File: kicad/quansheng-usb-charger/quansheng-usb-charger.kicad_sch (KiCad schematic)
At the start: 29 parts, among them J1 USB_C_Receptacle_USB2.0, U1 IP2326

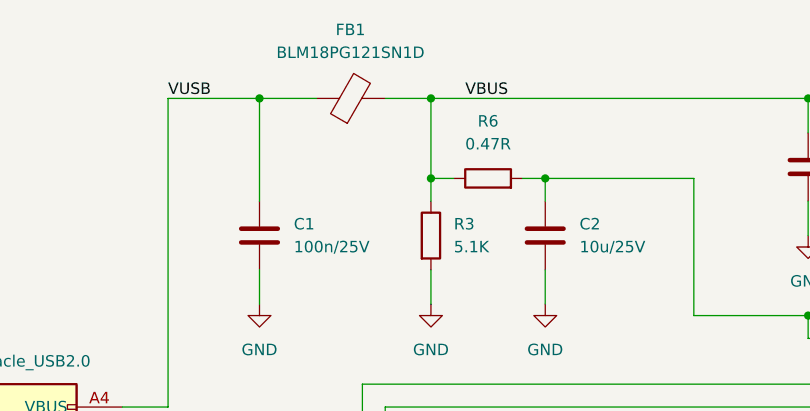
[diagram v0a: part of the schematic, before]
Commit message: Add JLCPCB files and README
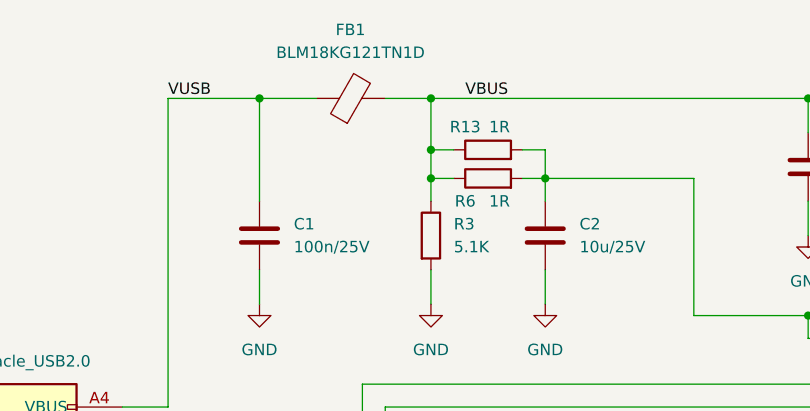
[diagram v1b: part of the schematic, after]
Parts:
- added R13: 1R, Resistor_SMD:R_0603_1608Metric, symbol Device:R
- C1, C4: LCSC (none) -> C14663
- C2, C3, C7, C8: LCSC (none) -> C15850
- C5, C6: LCSC (none) -> C45783
- FB1: value BLM18PG121SN1D -> BLM18KG121TN1D; LCSC (none) -> C85831
- J1: LCSC (none) -> C2988369
- L1: LCSC (none) -> C177247
- R1, R2, R3: LCSC (none) -> C23186
- R11: LCSC (none) -> C23196
- R12, R8, R9: LCSC (none) -> C25808
- R5, R7: LCSC (none) -> C21190
- R6: value 0.47R -> 1R; LCSC (none) -> C22936
- U1: LCSC (none) -> C2832094
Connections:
- net VBUS: now also R13.1
- net at C2.1, R6.2, U1.12 (EN)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: now also R13.2
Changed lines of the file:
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@@
   (junction (at 193.04 63.5) (diameter 0) (color 0 0 0 0)
   )
+  (junction (at 95.25 50.165) (diameter 0) (color 0 0 0 0)
+  )
   (junction (at 95.25 44.45) (diameter 0) (color 0 0 0 0)
   )
@@
     (stroke (width 0) (type default) (color 0 0 0 0))
   )
-  (wire (pts (xy 95.25 44.45) (xy 95.25 53.34))
+  (wire (pts (xy 95.25 44.45) (xy 95.25 50.165))
     (stroke (width 0) (type default) (color 0 0 0 0))
   )
@@
     (stroke (width 0) (type default) (color 0 0 0 0))
   )
+  (wire (pts (xy 95.25 50.165) (xy 97.79 50.165))
+    (stroke (width 0) (type default) (color 0 0 0 0))
+  )
   (wire (pts (xy 121.92 120.65) (xy 121.92 123.19))
     (stroke (width 0) (type default) (color 0 0 0 0))
@@
     (stroke (width 0) (type default) (color 0 0 0 0))
   )
+  (wire (pts (xy 105.41 50.165) (xy 107.95 50.165))
+    (stroke (width 0) (type default) (color 0 0 0 0))
+  )
   (wire (pts (xy 129.54 107.95) (xy 129.54 113.03))
     (stroke (width 0) (type default) (color 0 0 0 0))
@@
     (stroke (width 0) (type default) (color 0 0 0 0))
   )
+  (wire (pts (xy 107.95 50.165) (xy 107.95 53.34))
+    (stroke (width 0) (type default) (color 0 0 0 0))
+  )
   (wire (pts (xy 165.1 107.95) (xy 170.18 107.95))
     (stroke (width 0) (type default) (color 0 0 0 0))
@@
   )
   (wire (pts (xy 121.92 105.41) (xy 139.7 105.41))
+    (stroke (width 0) (type default) (color 0 0 0 0))
+  )
+  (wire (pts (xy 95.25 50.165) (xy 95.25 53.34))
     (stroke (width 0) (type default) (color 0 0 0 0))
   )
@@
       (effects (font (size 1.27 1.27)) hide)
     )
+    (property "LCSC" "C25808" (id 4) (at 124.46 115.5699 0)
+      (effects (font (size 1.27 1.27)) hide)
+    )
     (pin "1")
     (pin "2")
@@
       (effects (font (size 1.27 1.27)) hide)
     )
+    (property "LCSC" "C23186" (id 4) (at 82.55 106.6799 0)
+      (effects (font (size 1.27 1.27)) hide)
+    )
     (pin "1")
     (pin "2")
@@
       (effects (font (size 1.27 1.27)) hide)
     )
+    (property "LCSC" "C21190" (id 4) (at 102.87 146.0499 0)
+      (effects (font (size 1.27 1.27)) hide)
+    )
     (pin "1")
     (pin "2")
@@
       (effects (font (size 1.27 1.27)) hide)
     )
+    (property "LCSC" "C21190" (id 4) (at 109.22 115.5699 0)
+      (effects (font (size 1.27 1.27)) hide)
+    )
     (pin "1")
     (pin "2")
@@
     )
     (property "Datasheet" "~" (id 3) (at 203.2 72.39 0)
+      (effects (font (size 1.27 1.27)) hide)
+    )
+    (property "LCSC" "C15850" (id 4) (at 207.01 71.1199 0)
       (effects (font (size 1.27 1.27)) hide)
     )
@@
     (in_bom yes) (on_board yes) (fields_autoplaced)
     (property "Reference" "FB1" (id 0) (at 86.3092 36.83 90))
-    (property "Value" "BLM18PG121SN1D" (id 1) (at 86.3092 39.37 90))
+    (property "Value" "BLM18KG121TN1D" (id 1) (at 86.3092 39.37 90))
     (property "Footprint" "Inductor_SMD:L_0603_1608Metric" (id 2) (at 86.36 46.228 90)
       (effects (font (size 1.27 1.27)) hide)
     )
     (property "Datasheet" "~" (id 3) (at 86.36 44.45 0)
+      (effects (font (size 1.27 1.27)) hide)
+    )
+    (property "LCSC" "C85831" (id 4) (at 86.3092 36.83 0)
       (effects (font (size 1.27 1.27)) hide)
     )
@@
       (effects (font (size 1.27 1.27)) hide)
     )
+    (property "LCSC" "C45783" (id 4) (at 181.61 110.4899 0)
+      (effects (font (size 1.27 1.27)) hide)
+    )
     (pin "1")
     (pin "2")
@@
       (effects (font (size 1.27 1.27)) hide)
     )
+    (property "LCSC" "C45783" (id 4) (at 194.31 110.4899 0)
+      (effects (font (size 1.27 1.27)) hide)
+    )
     (pin "1")
     (pin "2")
@@
   )
   (symbol (lib_id "Device:R") (at 101.6 53.34 90) (unit 1)
-    (in_bom yes) (on_board yes) (fields_autoplaced)
-    (property "Reference" "R6" (id 0) (at 101.6 46.99 90))
-    (property "Value" "0.47R" (id 1) (at 101.6 49.53 90))
+    (in_bom yes) (on_board yes)
+    (property "Reference" "R6" (id 0) (at 99.06 55.88 90))
+    (property "Value" "1R" (id 1) (at 102.87 55.88 90))
     (property "Footprint" "Resistor_SMD:R_0603_1608Metric" (id 2) (at 101.6 55.118 90)
       (effects (font (size 1.27 1.27)) hide)
     )
     (property "Datasheet" "~" (id 3) (at 101.6 53.34 0)
+      (effects (font (size 1.27 1.27)) hide)
+    )
+    (property "LCSC" "C22936" (id 4) (at 99.06 55.88 0)
       (effects (font (size 1.27 1.27)) hide)
     )
@@
     (pin "1")
   )
+  (symbol (lib_id "Device:R") (at 101.6 50.165 90) (unit 1)
+    (in_bom yes) (on_board yes)
+    (property "Reference" "R13" (id 0) (at 99.06 47.625 90))
+    (property "Value" "1R" (id 1) (at 102.87 47.625 90))
+    (property "Footprint" "Resistor_SMD:R_0603_1608Metric" (id 2) (at 101.6 51.943 90)
+      (effects (font (size 1.27 1.27)) hide)
+    )
+    (property "Datasheet" "~" (id 3) (at 101.6 50.165 0)
+      (effects (font (size 1.27 1.27)) hide)
+    )
+    (property "LCSC" "C22936" (id 4) (at 99.06 47.625 0)
+      (effects (font (size 1.27 1.27)) hide)
+    )
+    (pin "1")
+    (pin "2")
+  )
   (symbol (lib_id "power:GND") (at 114.3 123.19 0) (unit 1)
     (in_bom yes) (on_board yes) (fields_autoplaced)
@@
     )
     (property "Datasheet" "https://www.usb.org/sites/default/files/documents/usb_type-c.zip" (id 3) (at 49.53 93.98 0)
+      (effects (font (size 1.27 1.27)) hide)
+    )
+    (property "LCSC" "C2988369" (id 4) (at 45.72 71.12 0)
       (effects (font (size 1.27 1.27)) hide)
     )
@@
       (effects (font (size 1.27 1.27)) hide)
     )
+    (property "LCSC" "C25808" (id 4) (at 139.7 115.5699 0)
+      (effects (font (size 1.27 1.27)) hide)
+    )
     (pin "1")
     (pin "2")
@@
     )
     (property "Datasheet" "" (id 3) (at 152.4 93.98 0)
+      (effects (font (size 1.27 1.27)) hide)
+    )
+    (property "LCSC" "C2832094" (id 4) (at 152.4 64.77 0)
       (effects (font (size 1.27 1.27)) hide)
     )
@@
       (effects (font (size 1.27 1.27)) hide)
     )
+    (property "LCSC" "C23196" (id 4) (at 132.08 86.36 0)
+      (effects (font (size 1.27 1.27)) hide)
+    )
     (pin "1")
     (pin "2")
@@
       (effects (font (size 1.27 1.27)) hide)
     )
+    (property "LCSC" "C15850" (id 4) (at 111.76 58.4199 0)
+      (effects (font (size 1.27 1.27)) hide)
+    )
     (pin "1")
     (pin "2")
@@
     )
     (property "Datasheet" "~" (id 3) (at 114.3 116.84 0)
+      (effects (font (size 1.27 1.27)) hide)
+    )
+    (property "LCSC" "C25808" (id 4) (at 116.84 115.5699 0)
       (effects (font (size 1.27 1.27)) hide)
     )
@@
       (effects (font (size 1.27 1.27)) hide)
     )
+    (property "LCSC" "C177247" (id 4) (at 151.13 38.1 0)
+      (effects (font (size 1.27 1.27)) hide)
+    )
     (pin "1")
     (pin "2")
@@
       (effects (font (size 1.27 1.27)) hide)
     )
+    (property "LCSC" "C23186" (id 4) (at 97.79 58.4199 0)
+      (effects (font (size 1.27 1.27)) hide)
+    )
     (pin "1")
     (pin "2")
@@
       (effects (font (size 1.27 1.27)) hide)
     )
+    (property "LCSC" "C15850" (id 4) (at 196.85 71.1199 0)
+      (effects (font (size 1.27 1.27)) hide)
+    )
     (pin "1")
     (pin "2")
@@
       (effects (font (size 1.27 1.27)) hide)
     )
+    (property "LCSC" "C14663" (id 4) (at 175.26 72.3899 0)
+      (effects (font (size 1.27 1.27)) hide)
+    )
     (pin "1")
     (pin "2")
@@
       (effects (font (size 1.27 1.27)) hide)
     )
+    (property "LCSC" "C23186" (id 4) (at 72.39 106.6799 0)
+      (effects (font (size 1.27 1.27)) hide)
+    )
     (pin "1")
     (pin "2")
@@
       (effects (font (size 1.27 1.27)) hide)
     )
+    (property "LCSC" "C14663" (id 4) (at 80.01 58.4199 0)
+      (effects (font (size 1.27 1.27)) hide)
+    )
     (pin "1")
     (pin "2")
@@
     )
     (property "Datasheet" "~" (id 3) (at 137.16 52.07 0)
+      (effects (font (size 1.27 1.27)) hide)
+    )
+    (property "LCSC" "C15850" (id 4) (at 140.97 50.7999 0)
       (effects (font (size 1.27 1.27)) hide)
     )
@@
     )
     (path "/36bf97d8-716f-4b33-a7e6-6eca368f4cd6"
-      (reference "FB1") (unit 1) (value "BLM18PG121SN1D") (footprint "Inductor_SMD:L_0603_1608Metric")
+      (reference "FB1") (unit 1) (value "BLM18KG121TN1D") (footprint "Inductor_SMD:L_0603_1608Metric")
     )
     (path "/925c6de2-4e65-45c6-b8d7-927003d2179d"
@@
     )
     (path "/56f50def-fab2-4a68-a043-a40a2cd7e978"
-      (reference "R6") (unit 1) (value "0.47R") (footprint "Resistor_SMD:R_0603_1608Metric")
+      (reference "R6") (unit 1) (value "1R") (footprint "Resistor_SMD:R_0603_1608Metric")
     )
     (path "/235f026d-5855-444f-8765-84a4fbd105a9"
@@
       (reference "R12") (unit 1) (value "120K") (footprint "Resistor_SMD:R_0603_1608Metric")
     )
+    (path "/8a0f8d63-3995-4e41-bf90-b71b0dd499a1"
+      (reference "R13") (unit 1) (value "1R") (footprint "Resistor_SMD:R_0603_1608Metric")
+    )
     (path "/9b3c58a7-a9b9-4498-abc0-f9f43e4f0292"

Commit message: Improve mechanical fit
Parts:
- TP3, TP4, TP5: footprint Connector_Wire:SolderWirePad_1x01_SMD_1x2mm -> TestPoint:TestPoint_THTPad_2.0x2.0mm_Drill1.0mm
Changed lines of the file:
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@@
       (effects (font (size 1.27 1.27)) (justify right))
     )
-    (property "Footprint" "Connector_Wire:SolderWirePad_1x01_SMD_1x2mm" (id 2) (at 82.55 153.67 0)
+    (property "Footprint" "TestPoint:TestPoint_THTPad_2.0x2.0mm_Drill1.0mm" (id 2) (at 82.55 153.67 0)
       (effects (font (size 1.27 1.27)) hide)
     )
@@
       (effects (font (size 1.27 1.27)) (justify right))
     )
-    (property "Footprint" "Connector_Wire:SolderWirePad_1x01_SMD_1x2mm" (id 2) (at 95.25 153.67 0)
+    (property "Footprint" "TestPoint:TestPoint_THTPad_2.0x2.0mm_Drill1.0mm" (id 2) (at 95.25 153.67 0)
       (effects (font (size 1.27 1.27)) hide)
     )
@@
       (effects (font (size 1.27 1.27)) (justify right))
     )
-    (property "Footprint" "Connector_Wire:SolderWirePad_1x01_SMD_1x2mm" (id 2) (at 107.95 153.67 0)
+    (property "Footprint" "TestPoint:TestPoint_THTPad_2.0x2.0mm_Drill1.0mm" (id 2) (at 107.95 153.67 0)
       (effects (font (size 1.27 1.27)) hide)
     )
@@
     )
     (path "/0b1e8daa-8973-47e8-8595-f8d419b95fe2"
-      (reference "TP3") (unit 1) (value "LEDG") (footprint "Connector_Wire:SolderWirePad_1x01_SMD_1x2mm")
+      (reference "TP3") (unit 1) (value "LEDG") (footprint "TestPoint:TestPoint_THTPad_2.0x2.0mm_Drill1.0mm")
     )
     (path "/782afd3c-6d72-4b56-b920-abee4f952e3f"
-      (reference "TP4") (unit 1) (value "LEDCOM") (footprint "Connector_Wire:SolderWirePad_1x01_SMD_1x2mm")
+      (reference "TP4") (unit 1) (value "LEDCOM") (footprint "TestPoint:TestPoint_THTPad_2.0x2.0mm_Drill1.0mm")
     )
     (path "/915ea535-5e0d-43e5-b5e7-328475f0c92a"
-      (reference "TP5") (unit 1) (value "LEDR") (footprint "Connector_Wire:SolderWirePad_1x01_SMD_1x2mm")
+      (reference "TP5") (unit 1) (value "LEDR") (footprint "TestPoint:TestPoint_THTPad_2.0x2.0mm_Drill1.0mm")
     )
     (path "/96508769-302b-4163-a45b-8e9837193608"

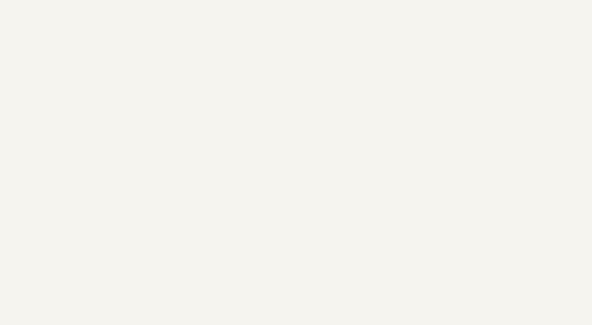
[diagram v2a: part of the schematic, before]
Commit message: Add Tooling Holes
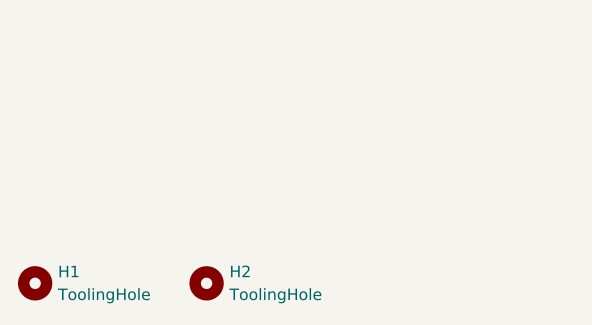
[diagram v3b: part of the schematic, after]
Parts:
- added H1, H2: ToolingHole, Project:TOOLING-HOLE, symbol Mechanical:MountingHole
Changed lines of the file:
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@@
     (pin "1")
+  )
+  (symbol (lib_id "Mechanical:MountingHole") (at 31.75 190.5 0) (unit 1)
+    (in_bom yes) (on_board yes) (fields_autoplaced)
+    (property "Reference" "H1" (id 0) (at 34.29 189.2299 0)
+      (effects (font (size 1.27 1.27)) (justify left))
+    )
+    (property "Value" "ToolingHole" (id 1) (at 34.29 191.7699 0)
+      (effects (font (size 1.27 1.27)) (justify left))
+    )
+    (property "Footprint" "Project:TOOLING-HOLE" (id 2) (at 31.75 190.5 0)
+      (effects (font (size 1.27 1.27)) hide)
+    )
+    (property "Datasheet" "~" (id 3) (at 31.75 190.5 0)
+      (effects (font (size 1.27 1.27)) hide)
+    )
   )
   (symbol (lib_id "power:GND") (at 177.8 123.19 0) (unit 1)
@@
     (pin "2")
   )
+  (symbol (lib_id "Mechanical:MountingHole") (at 50.8 190.5 0) (unit 1)
+    (in_bom yes) (on_board yes) (fields_autoplaced)
+    (property "Reference" "H2" (id 0) (at 53.34 189.2299 0)
+      (effects (font (size 1.27 1.27)) (justify left))
+    )
+    (property "Value" "ToolingHole" (id 1) (at 53.34 191.7699 0)
+      (effects (font (size 1.27 1.27)) (justify left))
+    )
+    (property "Footprint" "Project:TOOLING-HOLE" (id 2) (at 50.8 190.5 0)
+      (effects (font (size 1.27 1.27)) hide)
+    )
+    (property "Datasheet" "~" (id 3) (at 50.8 190.5 0)
+      (effects (font (size 1.27 1.27)) hide)
+    )
+  )
   (symbol (lib_id "Device:C") (at 76.2 59.69 180) (unit 1)
     (in_bom yes) (on_board yes) (fields_autoplaced)
@@
       (reference "FB1") (unit 1) (value "BLM18KG121TN1D") (footprint "Inductor_SMD:L_0603_1608Metric")
     )
+    (path "/805a692a-8a1c-4d5e-b6e4-5ecd40e54e5e"
+      (reference "H1") (unit 1) (value "ToolingHole") (footprint "Project:TOOLING-HOLE")
+    )
+    (path "/e0e633dd-67e3-4f45-9f73-00244cb82fe9"
+      (reference "H2") (unit 1) (value "ToolingHole") (footprint "Project:TOOLING-HOLE")
+    )
     (path "/925c6de2-4e65-45c6-b8d7-927003d2179d"
